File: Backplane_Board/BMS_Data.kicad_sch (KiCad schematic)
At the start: 5 parts, among them U5 PINA740AIREMR

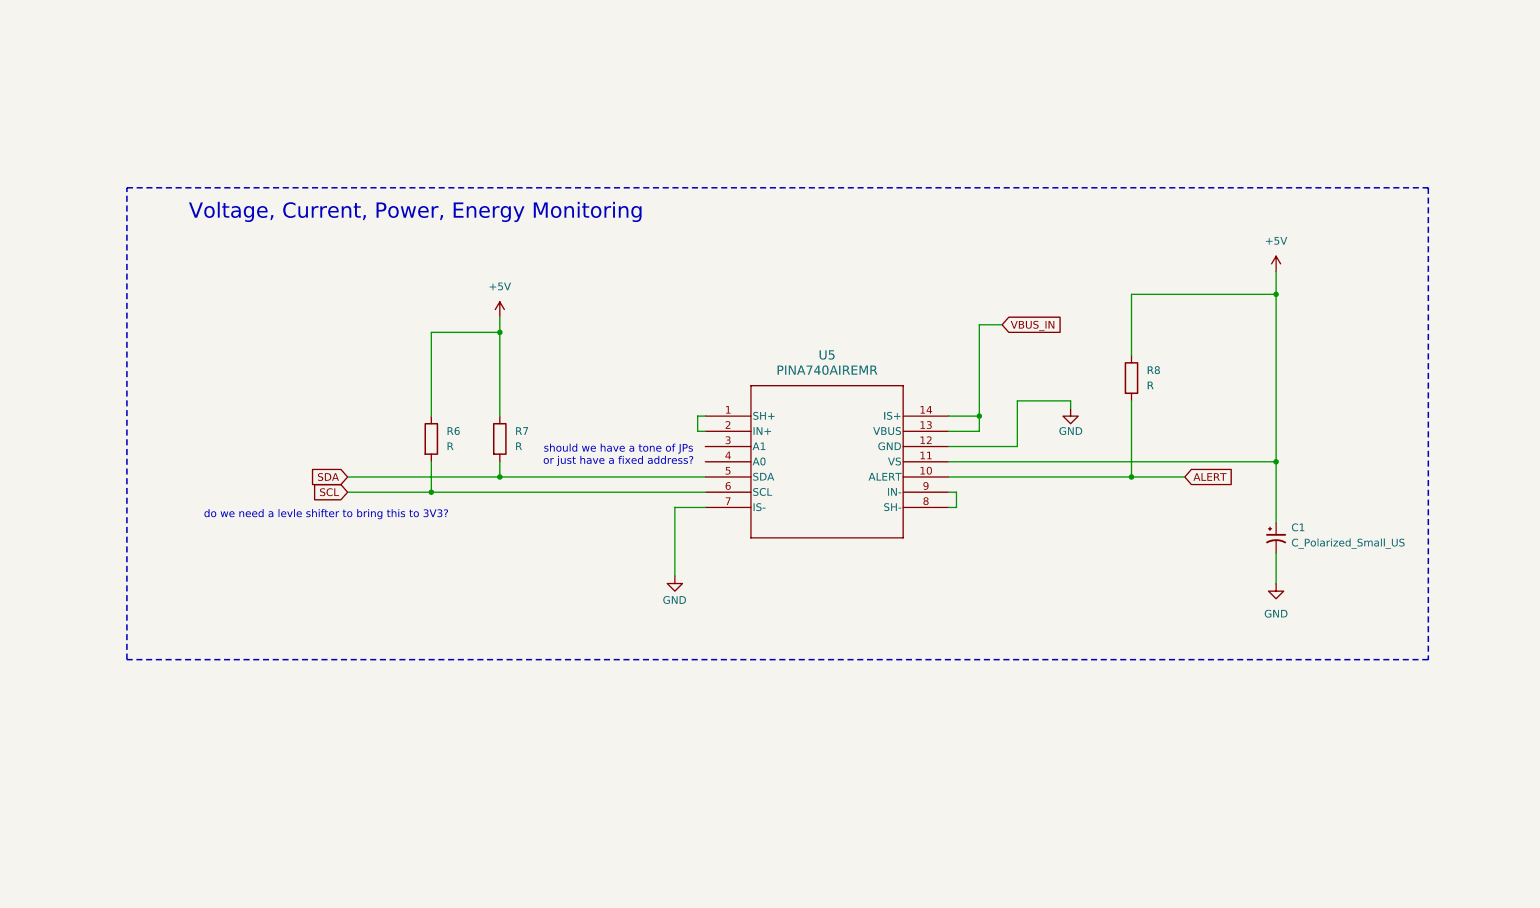
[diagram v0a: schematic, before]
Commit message: reviewed and cleaned up management ic
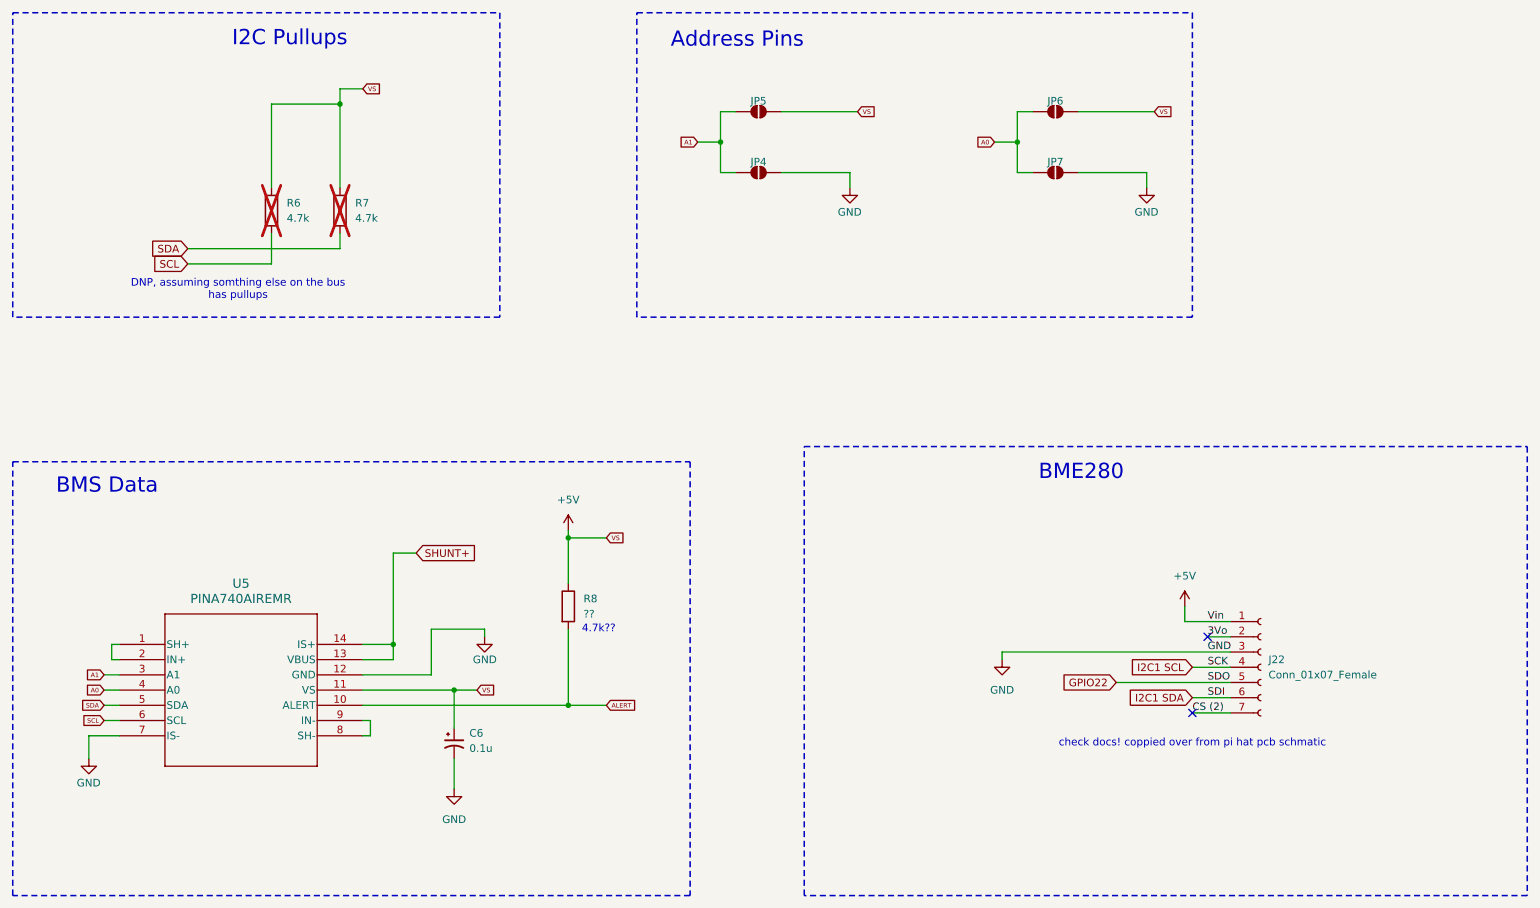
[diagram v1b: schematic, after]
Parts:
- removed C1: C_Polarized_Small_US, symbol Device:C_Polarized_Small_US
- added C6: 0.1u, symbol Device:C_Polarized_Small_US
- added J22: Conn_01x07_Female, Connector_PinSocket_2.54mm:PinSocket_1x07_P2.54mm_Vertical, symbol Connector:Conn_01x07_Female
- added JP4, JP5, JP6, JP7: SolderJumper_2_Open, symbol Jumper:SolderJumper_2_Open
- R6, R7: value R -> 4.7k; now not fitted
- R8: value R -> ??
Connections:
- net +5V: now also C6.1, J22.1 (Pin_1), JP5.2 (B), JP6.2 (B)
- net GND: now also C6.2, J22.3 (Pin_3), JP4.2 (B), JP7.2 (B)
- net A1: now reaches U5.3 (A1)
- net A1: now also JP4.1 (A), JP5.1 (A)
- net A0: now reaches U5.4 (A0)
- net A0: now also JP6.1 (A), JP7.1 (A)
- net VBUS_IN renamed SHUNT+
- new net 3Vo: J22.2 (Pin_2)
- new net CS (2): J22.7 (Pin_7)
- new net GPIO22: J22.5 (Pin_5)
- new net I2C1 SCL: J22.4 (Pin_4)
- new net I2C1 SDA: J22.6 (Pin_6)
- no-connect marks 0 -> 2
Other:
- note added: "4.7k??"
- note added: "Address Pins"
- note added: "BME280"
- note added: "BMS Data"
- note added: "DNP, assuming somthing else on the bus has pullups"
- note added: "I2C Pullups"
- note added: "check docs! coppied over from pi hat pcb schmatic"
- note removed: "Voltage, Current, Power, Energy Monitoring"
- note removed: "do we need a levle shifter to bring this to 3V3?"
- note removed: "should we have a tone of JPs or just have a fixed address?"
- moved on the sheet: R8, U5

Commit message: more updates
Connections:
- net I2C1 SCL is gone; now on net SCL: J22.4 (Pin_4)
- net I2C1 SDA is gone; now on net SDA: J22.6 (Pin_6)
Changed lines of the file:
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@@
 		)
 	)
-	(global_label "I2C1 SDA"
+	(global_label "SDA"
 		(shape input)
 		(at 218.44 132.08 180)
@@
 		)
 		(property "Intersheetrefs" "${INTERSHEET_REFS}"
-			(at 207.1974 132.0006 0)
+			(at 211.8867 132.08 0)
 			(effects
 				(font
@@
 		)
 	)
-	(global_label "I2C1 SCL"
+	(global_label "SCL"
 		(shape input)
 		(at 218.44 127 180)
@@
 		)
 		(property "Intersheetrefs" "${INTERSHEET_REFS}"
-			(at 207.2579 126.9206 0)
+			(at 211.9472 127 0)
 			(effects
 				(font

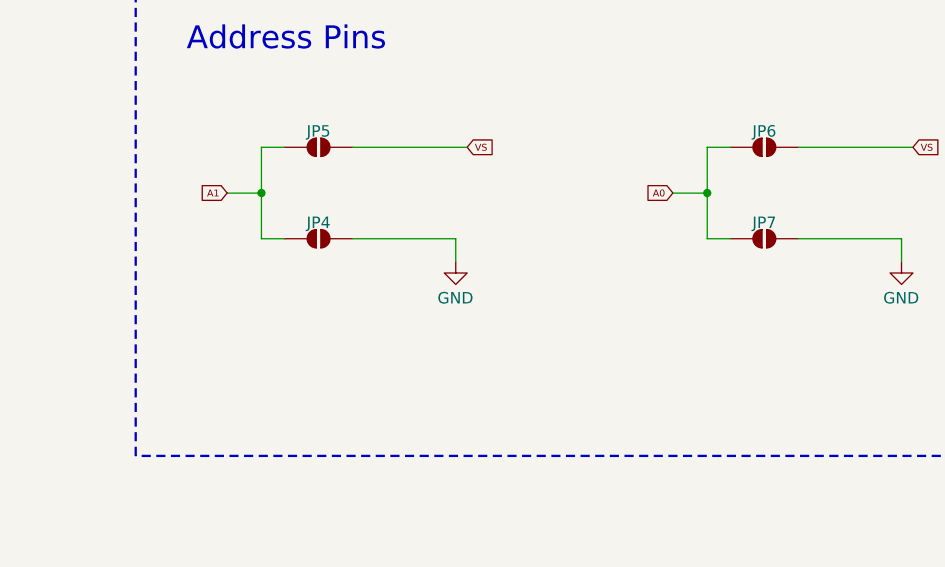
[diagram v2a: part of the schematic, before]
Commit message: added pico and 5v killSW
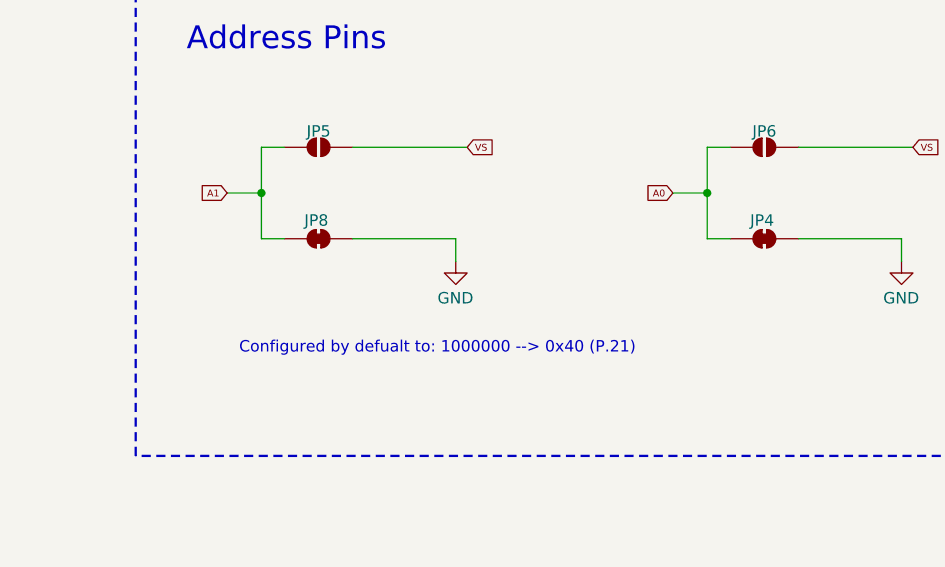
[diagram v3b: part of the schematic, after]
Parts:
- removed JP4, JP7: SolderJumper_2_Open, symbol Jumper:SolderJumper_2_Open
- added JP4, JP8: SolderJumper_2_Bridged, symbol Jumper:SolderJumper_2_Bridged
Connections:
- net A0: now also JP4.1 (A)
- net A1: now also JP8.1 (A)
- net GND: now also JP4.2 (B), JP8.2 (B)
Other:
- note added: "Configured by defualt to: 1000000 --> 0x40 (P.21)"
- title: (none) -> I2C Sensors
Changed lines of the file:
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@@
 	(paper "A4")
 	(title_block
-		(date "2024-09-30")
+		(title "I2C Sensors")
+		(date "2024-10-29")
 		(rev "1")
 		(company "Cabrillo Robtics")
@@
 			(font
 				(size 2.54 2.54)
+			)
+		)
+	)
+	(text "Configured by defualt to: 1000000 --> 0x40 (P.21)"
+		(exclude_from_sim no)
+		(at 159.258 56.642 0)
+		(effects
+			(font
+				(size 1.27 1.27)
 			)
 		)
@@
 				(path "/4484cfee-9e43-4cef-88b4-a8ca308542b4/829c4f27-479c-4774-bd79-d7d13a3cb460"
 					(reference "#PWR04")
-					(unit 1)
-				)
-			)
-		)
-	)
-	(symbol
-		(lib_id "Jumper:SolderJumper_2_Open")
-		(at 146.05 44.45 0)
-		(unit 1)
-		(exclude_from_sim yes)
-		(in_bom no)
-		(on_board yes)
-		(dnp no)
-		(property "Reference" "JP4"
-			(at 146.05 42.672 0)
-			(effects
-				(font
-					(size 1.27 1.27)
-				)
-			)
-		)
-		(property "Value" "SolderJumper_2_Open"
-			(at 146.05 40.64 0)
-			(effects
-				(font
-					(size 1.27 1.27)
-				)
-				(hide yes)
-			)
-		)
-		(property "Footprint" ""
-			(at 146.05 44.45 0)
-			(effects
-				(font
-					(size 1.27 1.27)
-				)
-				(hide yes)
-			)
-		)
-		(property "Datasheet" "~"
-			(at 146.05 44.45 0)
-			(effects
-				(font
-					(size 1.27 1.27)
-				)
-				(hide yes)
-			)
-		)
-		(property "Description" "Solder Jumper, 2-pole, open"
-			(at 146.05 44.45 0)
-			(effects
-				(font
-					(size 1.27 1.27)
-				)
-				(hide yes)
-			)
-		)
-		(pin "1"
-		)
-		(pin "2"
-		)
-		(instances
-			(project ""
-				(path "/4484cfee-9e43-4cef-88b4-a8ca308542b4/829c4f27-479c-4774-bd79-d7d13a3cb460"
-					(reference "JP4")
 					(unit 1)
 				)
@@
 	)
 	(symbol
+		(lib_id "Jumper:SolderJumper_2_Bridged")
+		(at 146.05 44.45 0)
+		(unit 1)
+		(exclude_from_sim yes)
+		(in_bom no)
+		(on_board yes)
+		(dnp no)
+		(property "Reference" "JP8"
+			(at 145.796 42.418 0)
+			(effects
+				(font
+					(size 1.27 1.27)
+				)
+			)
+		)
+		(property "Value" "SolderJumper_2_Bridged"
+			(at 146.05 40.64 0)
+			(effects
+				(font
+					(size 1.27 1.27)
+				)
+				(hide yes)
+			)
+		)
+		(property "Footprint" ""
+			(at 146.05 44.45 0)
+			(effects
+				(font
+					(size 1.27 1.27)
+				)
+				(hide yes)
+			)
+		)
+		(property "Datasheet" "~"
+			(at 146.05 44.45 0)
+			(effects
+				(font
+					(size 1.27 1.27)
+				)
+				(hide yes)
+			)
+		)
+		(property "Description" "Solder Jumper, 2-pole, closed/bridged"
+			(at 146.05 44.45 0)
+			(effects
+				(font
+					(size 1.27 1.27)
+				)
+				(hide yes)
+			)
+		)
+		(pin "2"
+		)
+		(pin "1"
+		)
+		(instances
+			(project ""
+				(path "/4484cfee-9e43-4cef-88b4-a8ca308542b4/829c4f27-479c-4774-bd79-d7d13a3cb460"
+					(reference "JP8")
+					(unit 1)
+				)
+			)
+		)
+	)
+	(symbol
 		(lib_id "Connector:Conn_01x07_Female")
 		(at 229.87 127 0)
@@
 	)
 	(symbol
-		(lib_id "Jumper:SolderJumper_2_Open")
-		(at 195.58 44.45 0)
-		(unit 1)
-		(exclude_from_sim yes)
-		(in_bom no)
-		(on_board yes)
-		(dnp no)
-		(property "Reference" "JP7"
-			(at 195.58 42.672 0)
-			(effects
-				(font
-					(size 1.27 1.27)
-				)
-			)
-		)
-		(property "Value" "SolderJumper_2_Open"
-			(at 195.58 40.64 0)
-			(effects
-				(font
-					(size 1.27 1.27)
-				)
-				(hide yes)
-			)
-		)
-		(property "Footprint" ""
-			(at 195.58 44.45 0)
-			(effects
-				(font
-					(size 1.27 1.27)
-				)
-				(hide yes)
-			)
-		)
-		(property "Datasheet" "~"
-			(at 195.58 44.45 0)
-			(effects
-				(font
-					(size 1.27 1.27)
-				)
-				(hide yes)
-			)
-		)
-		(property "Description" "Solder Jumper, 2-pole, open"
-			(at 195.58 44.45 0)
-			(effects
-				(font
-					(size 1.27 1.27)
-				)
-				(hide yes)
-			)
-		)
-		(pin "1"
-		)
-		(pin "2"
-		)
-		(instances
-			(project "Backplane_Board"
-				(path "/4484cfee-9e43-4cef-88b4-a8ca308542b4/829c4f27-479c-4774-bd79-d7d13a3cb460"
-					(reference "JP7")
-					(unit 1)
-				)
-			)
-		)
-	)
-	(symbol
 		(lib_id "power:+5V")
 		(at 114.3 104.14 0)
@@
 					(unit 1)
 				)
+			)
+		)
+	)
+	(symbol
+		(lib_id "Jumper:SolderJumper_2_Bridged")
+		(at 195.58 44.45 0)
+		(unit 1)
+		(exclude_from_sim yes)
+		(in_bom no)
+		(on_board yes)
+		(dnp no)
+		(property "Reference" "JP4"
+			(at 195.326 42.418 0)
+			(effects
+				(font
+					(size 1.27 1.27)
+				)
+			)
+		)
+		(property "Value" "SolderJumper_2_Bridged"
+			(at 195.58 40.64 0)
+			(effects
+				(font
+					(size 1.27 1.27)
+				)
+				(hide yes)
+			)
+		)
+		(property "Footprint" ""
+			(at 195.58 44.45 0)
+			(effects
+				(font
+					(size 1.27 1.27)
+				)
+				(hide yes)
+			)
+		)
+		(property "Datasheet" "~"
+			(at 195.58 44.45 0)
+			(effects
+				(font
+					(size 1.27 1.27)
+				)
+				(hide yes)
+			)
+		)
+		(property "Description" "Solder Jumper, 2-pole, closed/bridged"
+			(at 195.58 44.45 0)
+			(effects
+				(font
+					(size 1.27 1.27)
+				)
+				(hide yes)
+			)
+		)
+		(pin "2"
+		)
+		(pin "1"
+		)
+		(instances
+			(project "Backplane_Board"
+				(path "/4484cfee-9e43-4cef-88b4-a8ca308542b4/829c4f27-479c-4774-bd79-d7d13a3cb460"
+					(reference "JP4")
+					(unit 1)
+				)

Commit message: ready for final schmatic review
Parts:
- R8: value ?? -> 4.7k
- U5: footprint VQFN14_REM_TEX -> PINA740AIREMR:INA740BIREMR
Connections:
- net +5V: no longer JP5.2 (B), JP6.2 (B)
- net SCL: now also JP5.2 (B), JP6.2 (B)
- net 3Vo: no longer names the net of J22.2 (Pin_2)
- net CS (2): no longer names the net of J22.7 (Pin_7)
- net GPIO22: no longer names the net of J22.5 (Pin_5)
- no-connect marks 2 -> 3
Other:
- note added: "-I2C and alert are currently being pulled up to the 5V bus. This is bad pratice, becasue the pico uses 3.3V logic. - We should either pull up to 3.3V or add a level shifter IC? - Could have the I2C pullups go to the 3V3 bus of the pico insted. That should fix it?"
- note added: "Note: This seems kindof dangrous and seems like it could lead to a high risk of us shorting the 5V bus to GND. I wonder if we want to consider a diffrent pull up for the addtion of more address opptions?"
- note added: "VS = 5V"

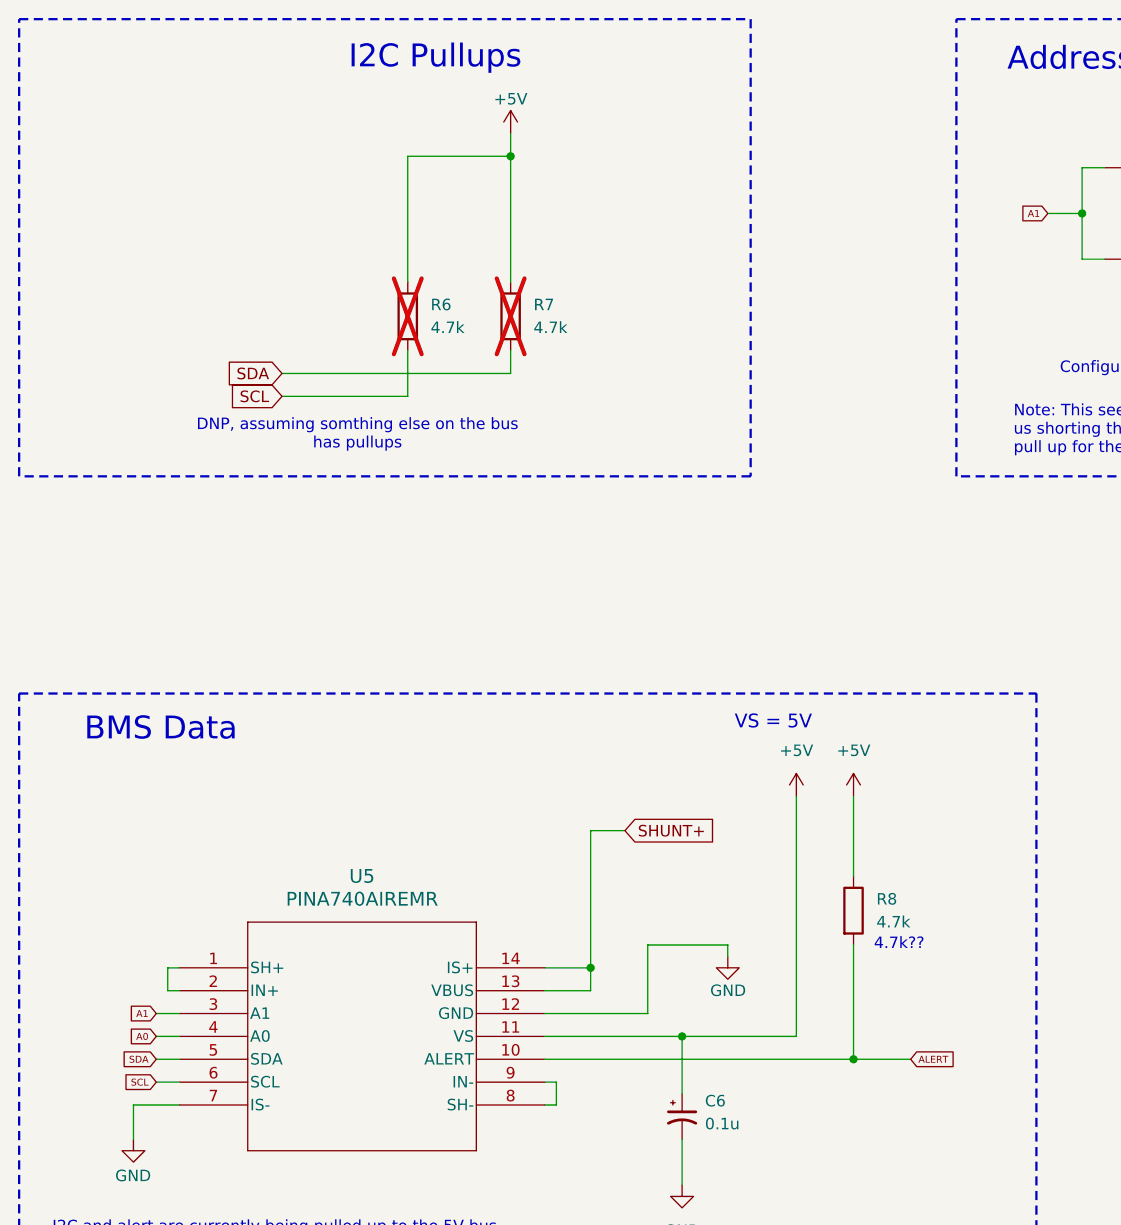
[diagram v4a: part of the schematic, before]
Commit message: updated i2c pullups to 3V3 logic, not isolator needed
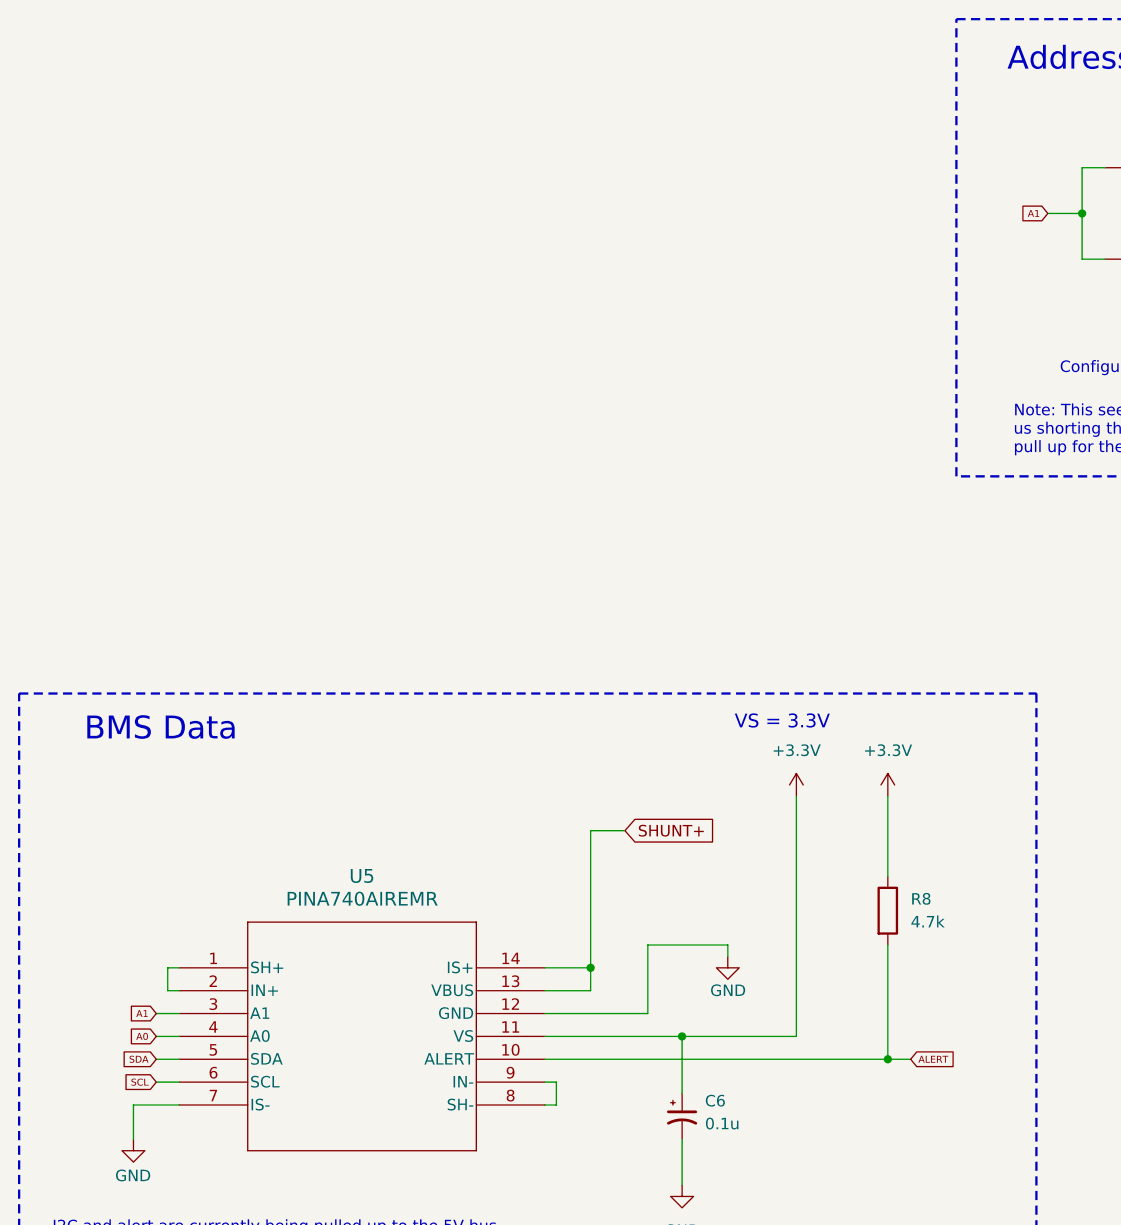
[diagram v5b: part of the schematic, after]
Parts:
- removed R6, R7: 4.7k, symbol Device:R
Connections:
- net +5V: no longer C6.1, R8.1, U5.11 (VS)
- new net +3.3V: C6.1, R8.1, U5.11 (VS)
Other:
- note added: "VS = 3.3V"
- note removed: "4.7k??"
- note removed: "DNP, assuming somthing else on the bus has pullups"
- note removed: "I2C Pullups"
- note removed: "VS = 5V"
- moved on the sheet: R8
